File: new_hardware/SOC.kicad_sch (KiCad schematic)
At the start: 88 parts, among them J3 TF01-A, P1 USB-TYPE-C-018, P2 WF24LTYAJDNN0#, Q1 Q_NMOS_DSG, SW2 K2-1156SP-F5SW-05, SW3 K2-1156SP-F5SW-05, SW4 K2-1156SP-F5SW-05, SW5 K2-1156SP-F5SW-05, SW6 K2-1156SP-F5SW-05, SW7 GT-TC054A-H035-L1, SW8 GT-TC054A-H035-L1, U2 F133, U8 USBLC6-2SC6, U9 MX25L25645GM2I-08G, Y1 12.88727

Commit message: xxxx
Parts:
- removed Q1: Q_NMOS_DSG, symbol Device:Q_NMOS_DSG
- added H1, H2, H3, H4: MountingHole, MountingHole:MountingHole_2.2mm_M2_DIN965_Pad, symbol Mechanical:MountingHole
- added Q1: 2N7002K, rlib_passive:SOT-23, symbol rlib_passive:2N7002K
- C5: renamed from C19; value 100n -> 18p
- C6: renamed from C35; value 100n -> 18p
- TP1: renamed from TP8; footprint (none) -> TestPoint:TestPoint_Pad_D1.0mm
- TP10: renamed from TP13; footprint (none) -> TestPoint:TestPoint_Pad_D1.0mm
- TP11, TP12: renamed from TP?; footprint (none) -> TestPoint:TestPoint_Pad_D1.0mm
- TP2: renamed from TP17; footprint (none) -> TestPoint:TestPoint_Pad_D1.0mm
- TP3: renamed from TP18; footprint (none) -> TestPoint:TestPoint_Pad_D1.0mm
- TP4: renamed from TP19; footprint (none) -> TestPoint:TestPoint_Pad_D1.0mm
- TP5: renamed from TP9; footprint (none) -> TestPoint:TestPoint_Pad_D1.0mm
- TP6: footprint (none) -> TestPoint:TestPoint_Pad_D1.0mm
- TP7: renamed from TP10; footprint (none) -> TestPoint:TestPoint_Pad_D1.0mm
- TP8: renamed from TP11; footprint (none) -> TestPoint:TestPoint_Pad_D1.0mm
- TP9: renamed from TP12; footprint (none) -> TestPoint:TestPoint_Pad_D1.0mm
- gave numbers to parts that had none: 1
- renumbered C15 to C1, C22 to C10, C23 to C11, C24 to C12, C25 to C13, C26 to C14, C27 to C15, C28 to C16, C29 to C17, C33 to C18, C30 to C19, C67 to C2, C60 to C20, C31 to C21, C34 to C22, C32 to C23, C70 to C24, C71 to C25, C47 to C26, C66 to C27, C17 to C3, C18 to C4, C36 to C7, C20 to C8, C21 to C9, D4 to D1, D5 to D2, D6 to D3, D7 to D4, D8 to D5, D9 to D6, D10 to D7, F2 to F1, J3 to J1, L9 to L1, P2 to P1, P1 to P2, R38 to R1, R30 to R10, R31 to R11, R32 to R12, R33 to R13, R34 to R14, R35 to R15, R36 to R16, R10 to R17, R37 to R18, R43 to R19, R39 to R2, R44 to R20, R13 to R21, R12 to R22, R11 to R3, R40 to R4, R3 to R5, R7 to R6, R8 to R7, R9 to R8, R29 to R9, SW2 to SW1, SW3 to SW2, SW4 to SW3, SW5 to SW4, SW6 to SW5, SW7 to SW6, SW8 to SW7, U2 to U1, U8 to U2, U9 to U3
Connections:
- net FLASH_SPI_MISO is gone; now on net FLASH_SPI_CS: R21.1, TP11.1, U1.16 (PC5), U3.2 (DO(IO1))
- net GND: now also Q1.2 (S)
- net I2C_SCK: now also U1.3 (PG8)
- net I2C_SDA: now also U1.4 (PG9)
- net LCD_EN: now also U1.2 (PG7); no longer U1.4 (PG9)
- net HP_PLUG: now reaches U1.71 (PD14)
- net at R1.2: now also Q1.3 (D)
- net at R2.1, R4.1: now also Q1.1 (G)
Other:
- moved on the sheet: JP1, R17, R21, TP6

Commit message: changed lcd interface and layout is partly made
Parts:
- removed C16, C3, C7: 100n, rlib_passive:C_0603_1608Metric, symbol rlib_passive:C
- C12: value 100n -> 10u
- C13: value 100n -> 1u
- H1, H2, H3, H4: footprint MountingHole:MountingHole_2.2mm_M2_DIN965_Pad -> MountingHole:MountingHole_2.5mm_Pad_Via
- JP1, JP2: footprint (none) -> Jumper:SolderJumper-2_P1.3mm_Open_TrianglePad1.0x1.5mm
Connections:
- net +3V3: no longer C15.1, C17.1, C19.1, U1.116 (VDD-CORE0), U1.117 (VDD-CORE1), U1.51 (VDD-SYS0), U1.81 (VDD-SYS2)
- net FLASH_SPI_CS: no longer R21.1, TP11.1, U1.16 (PC5), U3.2 (DO(IO1))
- net GND: now also P1.23 (DB9), P1.24 (DB10), P1.25 (DB11), P1.26 (DB12), P1.27 (DB13), P1.28 (DB14), P1.29 (DB15), U1.129 (GND)
- net LCD_D0: no longer P1.14 (DB0)
- net LCD_D1: no longer P1.15 (DB1)
- net LCD_D10: now also P1.19 (DB5); no longer P1.24 (DB10)
- net LCD_D11: now also P1.20 (DB6); no longer P1.25 (DB11)
- net LCD_D12: now also P1.21 (DB7); no longer P1.26 (DB12)
- net LCD_D13: no longer P1.27 (DB13)
- net LCD_D14: no longer P1.28 (DB14)
- net LCD_D15: no longer P1.29 (DB15)
- net LCD_D2: no longer P1.16 (DB2)
- net LCD_D3: now also P1.14 (DB0); no longer P1.17 (DB3)
- net LCD_D4: now also P1.15 (DB1); no longer P1.18 (DB4)
- net LCD_D5: now also P1.16 (DB2); no longer P1.19 (DB5)
- net LCD_D6: now also P1.17 (DB3); no longer P1.20 (DB6)
- net LCD_D7: now also P1.18 (DB4); no longer P1.21 (DB7)
- net LCD_D8: no longer P1.22 (DB8)
- net LCD_D9: no longer P1.23 (DB9)
- net LCD_EN: no longer P1.30 (RESET), R3.1
- net CHR_IRQ: now reaches U1.31 (PE13)
- net +1V8B: now reaches TP7.1
- net +1V8B: now also C12.1, C13.1, C14.1, C9.1, U1.30 (LDOB-OUT), U1.48 (VCC-DRAM0), U1.49 (VCC-DRAM1), U1.50 (VDD18-DRAM)
- net +1V8 renamed +1V8A
- net +1V8A: no longer C12.1, C13.1, C14.1, C9.1, U1.30 (LDOB-OUT), U1.48 (VCC-DRAM0), U1.49 (VCC-DRAM1), U1.50 (VDD18-DRAM)
- new net: P1.30 (RESET), R3.1
- new net +0V9: C15.1, C17.1, C19.1, U1.116 (VDD-CORE0), U1.117 (VDD-CORE1), U1.51 (VDD-SYS0), U1.81 (VDD-SYS2)
- new net FLASH_SPI_MISO: R21.1, TP11.1, U1.16 (PC5), U3.2 (DO(IO1))
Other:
- moved on the sheet: C17, TP7

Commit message: some fucking changes
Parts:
- removed C20: 100n, rlib_passive:C_0603_1608Metric, symbol rlib_passive:C
- removed L1: L, rlib_passive:INDC2520X120N, symbol rlib_passive:L
- added C3: 100n, rlib_passive:C_0603_1608Metric, symbol rlib_passive:C
- added D13, D14: PESD3V3L1BA, rlib_passive:D_SOD-323F, symbol rlib_passive:PESD3V3L1BA
- added FB1: FerriteBead, rlib_passive:INDC2520X120N, symbol rlib_passive:FerriteBead
- added R51, R52: 27, rlib_passive:R_0603_1608Metric, symbol rlib_passive:R
- added R53, R56, R57: 10k, rlib_passive:R_0603_1608Metric, symbol rlib_passive:R
- C1, C10, C11, C14, C15, C17, C18, C19, C2, C21, C22, C23, C24, C25, C26, C27: LCSC partnumber (none) -> C45000
- C12: LCSC partnumber (none) -> C91606; Mnfct. partnumber GRM188R71C104KA01D -> GRM188R61E106MA73D
- C13: LCSC partnumber (none) -> C77386; Mnfct. partnumber GRM188R71C104KA01D -> GRM188R61H105KAALD
- C4, C8: LCSC partnumber (none) -> C91606; Manufacturer (none) -> Murata; Mnfct. partnumber (none) -> GRM188R61E106MA73D
- C5, C6: LCSC partnumber (none) -> C106202; Manufacturer Murata -> YAGEO; Mnfct. partnumber GRM188R71C104KA01D -> CC0402JRNPO9BN180; TC (none) -> 1%
- C9: LCSC partnumber (none) -> C162273; Manufacturer (none) -> Murata; Mnfct. partnumber (none) -> GRM188R61H225KE11D
- D1, D2, D3, D4, D5, D6, D7, D8: LCSC partnumber (none) -> C2827682; Manufacturer (none) -> TECH PUBLIC; Mnfct. partnumber (none) -> PESD3V3L1BA
- JP1, JP2, TP1, TP10, TP11, TP12, TP2, TP3, TP4, TP6, TP9: now left out of the parts list
- P1: LCSC partnumber (none) -> -; Manufacturer (none) -> Winstar; Mnfct. partnumber (none) -> WF24LTYAJDNN0#
- R10, R11, R12, R13, R14, R15, R16, R17, R18, R2, R21, R22, R3, R5, R7, R8, R9: LCSC partnumber (none) -> C217687; Manufacturer (none) -> Viking Tech; Mnfct. partnumber (none) -> ARG03FTC1002; Tolerance (none) -> 1%
- R19, R20: LCSC partnumber (none) -> C217926; Manufacturer (none) -> Viking Tech; Mnfct. partnumber (none) -> ARG03FTC0270; Tolerance (none) -> 1%
- R4: LCSC partnumber (none) -> C217683; Manufacturer (none) -> Viking Tech; Mnfct. partnumber (none) -> ARG03FTC1000; Tolerance (none) -> 1%
- R6: value 50 -> 100; LCSC partnumber (none) -> C217683; Manufacturer (none) -> Viking Tech; Mnfct. partnumber (none) -> ARG03FTC1000; Tolerance (none) -> 1%
- SW6, SW7: LCSC partnumber (none) -> C778158
- U1: LCSC partnumber (none) -> -; Manufacturer (none) -> Allwinner; Mnfct. partnumber (none) -> F133-A
- U2: LCSC Partnumber C7519 -> (none); LCSC partnumber (none) -> C7519; Manufacturer (none) -> STMicroelectronics; Mnfct. partnumber (none) -> USBLC6-2SC6
- Y1: LCSC partnumber (none) -> -; Manufacturer (none) -> Geyer Electronic; Mnfct. partnumber (none) -> 12.88727
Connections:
- net LCD_D0 is gone; now on net I2C_SDA: U1.86 (PB2)
- net LCD_D1 is gone; now on net I2C_SCK: U1.85 (PB3)
- net LCD_D8 is gone; now on net I2S_DOUT: U1.84 (PB4)
- net LCD_D9 is gone; now on net I2S_BCLK: U1.82 (PB5)
- net +3V3: now also R56.1, R57.1
- net CHR_IRQ: now also U1.32 (PE12); no longer U1.31 (PE13)
- net DEBUG_UART_RX: now also R51.1; no longer TP9.1
- net DEBUG_UART_TX: now also R52.2; no longer TP10.1
- net GND: now also P1.22 (DB8), P1.34 (DB16), P1.35 (DB17), C3.2, D13.1 (A1), D14.1 (A1), R53.2
- net I2C_SCK: no longer U1.3 (PG8)
- net I2C_SDA: no longer U1.4 (PG9)
- net I2S_BCLK: no longer U1.125 (PG13)
- net I2S_DOUT: no longer U1.127 (PG15)
- net I2S_LRCK: now also U1.80 (PB6); no longer U1.124 (PG12)
- net I2S_MCLK: now also U1.79 (PB7); no longer U1.6 (PG11)
- net KEYS: now also D1.2 (A2), C3.1
- net LCD_EN: now also P1.30 (RESET), R3.1, U1.52 (PD22); no longer U1.2 (PG7)
- net LCD_PWM: now also U1.38 (PE9); no longer U1.5 (PG10)
- net SDC_CLK: now also R18.2, U1.9 (PF2); no longer U1.120 (PG0)
- net SDC_CMD: now also R16.2, U1.10 (PF3); no longer U1.118 (PG1)
- net SDC_D0: now also U1.8 (PF1), R56.2; no longer R16.2, U1.119 (PG2)
- net SDC_D1: now also U1.7 (PF0), R57.2; no longer R18.2, U1.121 (PG3)
- net SDC_D2: now also U1.12 (PF5); no longer U1.123 (PG4)
- net SDC_D3: now also U1.11 (PF4); no longer U1.122 (PG5)
- net SDC_PLUG: now also U1.6 (PG11); no longer U1.1 (PG6)
- net VBUS: now also FB1.1
- net at C25.1, F1.1: now also FB1.2
- net at R13.2, SW7.1: no longer D1.2 (A2)
- net at U1.47 (DZQ): now also R53.1
- new net: D13.2 (A2), R51.2, TP9.1
- new net: D14.2 (A2), R52.1, TP10.1
- new net WIFI_SDIO_CLK: U1.120 (PG0)
- new net WIFI_SDIO_CMD: U1.118 (PG1)
- new net WIFI_SDIO_D0: U1.119 (PG2)
- new net WIFI_SDIO_D1: U1.121 (PG3)
- new net WIFI_SDIO_D2: U1.122 (PG5)
- new net WIFI_SDIO_D3: U1.123 (PG4)
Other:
- moved on the sheet: C19, C24, JP1, R10, R11, R12, R13, R5, R6, R7, R9, SW1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

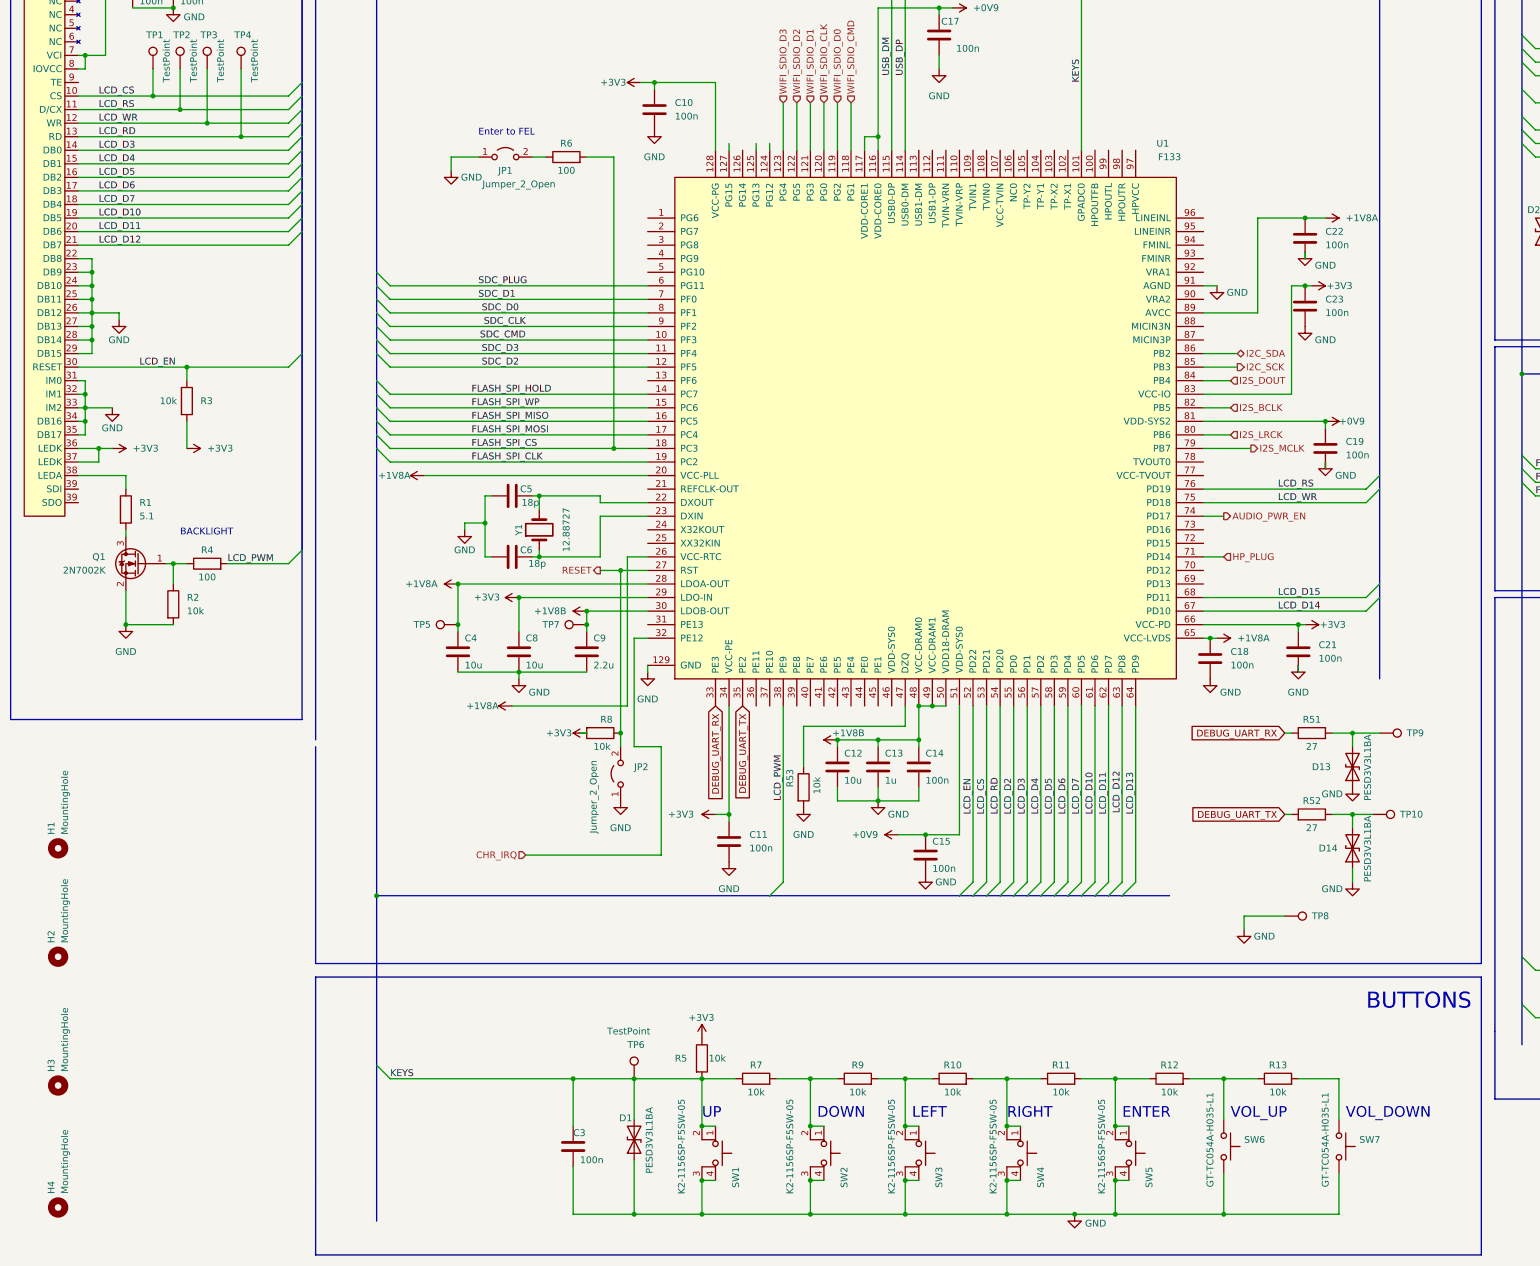
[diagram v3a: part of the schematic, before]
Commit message: device tree is changed
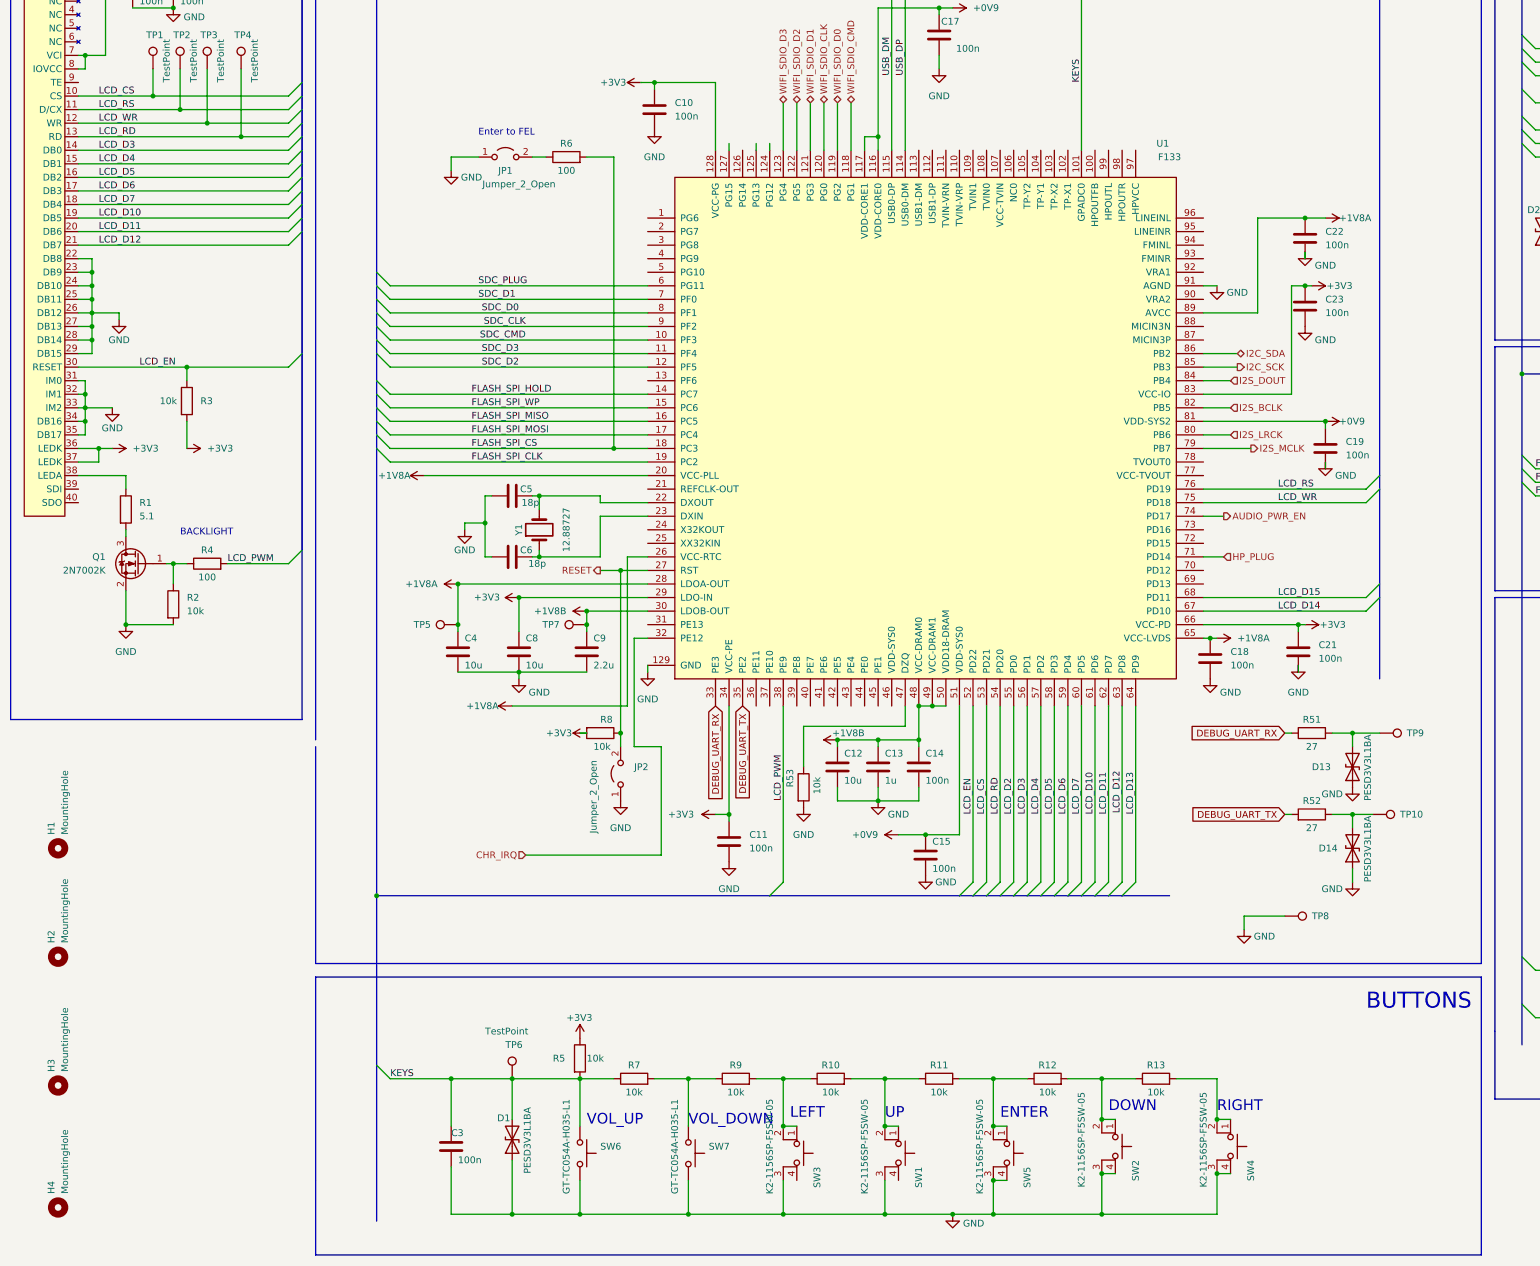
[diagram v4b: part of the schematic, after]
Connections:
- net GND: no longer SW1.4 (A), SW3.4 (A)
- net KEYS: now also SW6.1; no longer SW1.1, SW1.2
- net at R10.2, R11.1: now also SW1.1, SW1.2; no longer SW4.1, SW4.2
- net at SW7.1: now also R7.2, R9.1; no longer R13.2
- net at SW2.1, SW2.2: now also R12.2, R13.1; no longer R7.2, R9.1
- new net: R13.2, SW4.1, SW4.2
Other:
- moved on the sheet: C3, D1, R10, R11, R12, R13, R5, R7, R9, SW1, SW2, SW3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

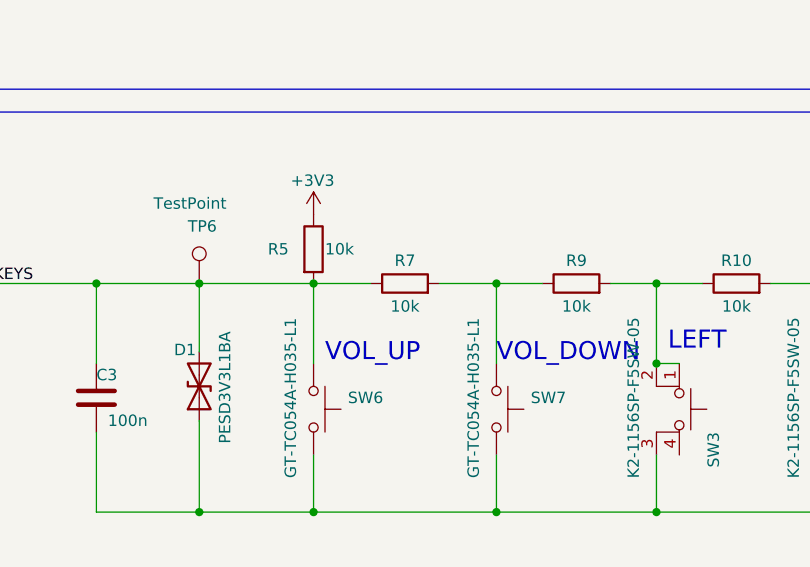
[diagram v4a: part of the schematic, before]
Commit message: removed some unused files
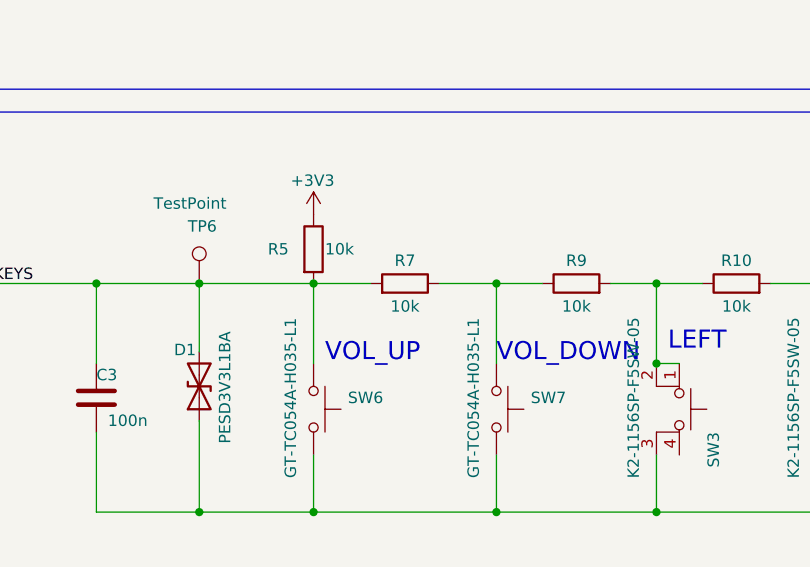
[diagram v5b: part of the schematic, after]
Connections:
- net KEYS: now also R7.2; no longer R7.1
- net at R9.1, SW7.1: now also R7.1; no longer R7.2
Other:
- moved on the sheet: R7
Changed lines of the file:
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@@
     (pin "1")
   )
-  (symbol (lib_id "rlib_passive:R") (at 130.81 246.38 90) (unit 1)
+  (symbol (lib_id "rlib_passive:R") (at 130.81 246.38 270) (mirror x) (unit 1)
     (in_bom yes) (on_board yes)
     (property "Reference" "R7" (id 0) (at 130.81 243.84 90))
